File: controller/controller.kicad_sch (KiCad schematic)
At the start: 95 parts, among them J11 Conn_ARM_JTAG_SWD_10, J12 GRPB072VWQS-RC, J13 GRPB072VWQS-RC, J15 Conn_01x03_Pin, J6 USB_C_Receptacle_USB2.0_16P, J7 USB_C_Receptacle_USB2.0_16P, J8 GRPB072VWQS-RC, J9 GRPB072VWQS-RC, Q1 BSS138, Q2 BSS138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

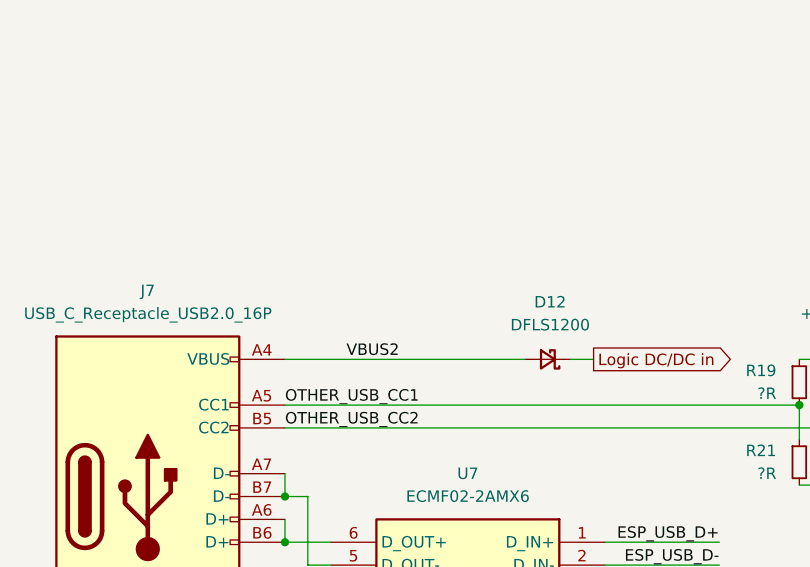
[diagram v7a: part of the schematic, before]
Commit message: Controller - Cleanup and improve silkscreen
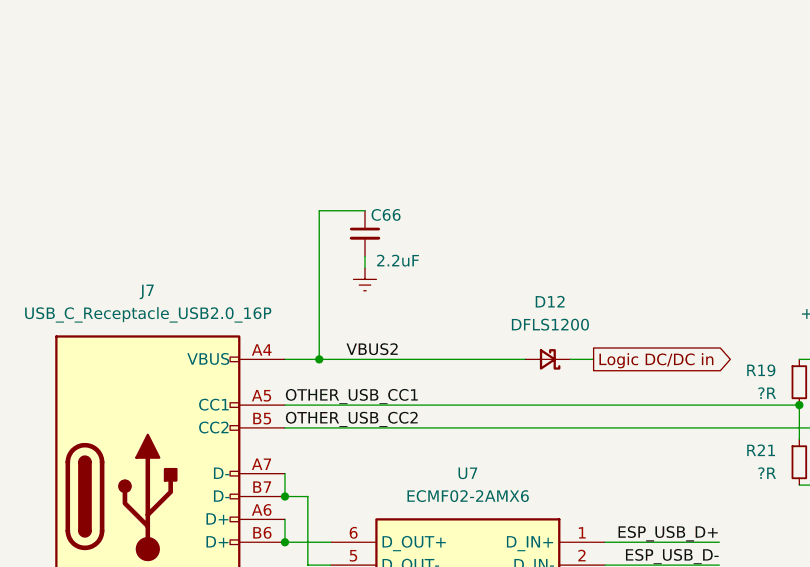
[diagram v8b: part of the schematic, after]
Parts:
- added C66: 2.2uF, Capacitor_SMD:C_0603_1608Metric, symbol Device:C_Small
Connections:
- net Earth: now also C66.2
- net VBUS2: now also C66.1
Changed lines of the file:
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@@
 	)
 	(junction
+		(at 48.26 222.25)
+		(diameter 0)
+		(color 0 0 0 0)
+	)
+	(junction
 		(at 334.01 165.1)
 		(diameter 0)
@@
 	(wire
 		(pts
+			(xy 53.34 210.82) (xy 53.34 212.09)
+		)
+		(stroke
+			(width 0)
+			(type default)
+		)
+	)
+	(wire
+		(pts
 			(xy 147.32 34.29) (xy 163.83 34.29)
 		)
@@
 	(wire
 		(pts
-			(xy 44.45 222.25) (xy 71.12 222.25)
+			(xy 44.45 222.25) (xy 48.26 222.25)
 		)
 		(stroke
@@
 	(wire
 		(pts
+			(xy 53.34 205.74) (xy 48.26 205.74)
+		)
+		(stroke
+			(width 0)
+			(type default)
+		)
+	)
+	(wire
+		(pts
 			(xy 33.02 66.04) (xy 48.26 66.04)
 		)
@@
 	(wire
 		(pts
+			(xy 48.26 205.74) (xy 48.26 222.25)
+		)
+		(stroke
+			(width 0)
+			(type default)
+		)
+	)
+	(wire
+		(pts
 			(xy 45.72 349.25) (xy 45.72 350.52)
 		)
@@
 	(wire
 		(pts
+			(xy 48.26 222.25) (xy 71.12 222.25)
+		)
+		(stroke
+			(width 0)
+			(type default)
+		)
+	)
+	(wire
+		(pts
 			(xy 278.13 275.59) (xy 278.13 278.13)
 		)
@@
 	)
 	(symbol
+		(lib_id "Device:C_Small")
+		(at 53.34 208.28 0)
+		(unit 1)
+		(exclude_from_sim no)
+		(in_bom yes)
+		(on_board yes)
+		(dnp no)
+		(property "Reference" "C66"
+			(at 57.404 206.248 0)
+			(effects
+				(font
+					(size 1.27 1.27)
+				)
+				(justify right)
+			)
+		)
+		(property "Value" "2.2uF"
+			(at 59.436 211.328 0)
+			(effects
+				(font
+					(size 1.27 1.27)
+				)
+				(justify right)
+			)
+		)
+		(property "Footprint" "Capacitor_SMD:C_0603_1608Metric"
+			(at 53.34 208.28 0)
+			(effects
+				(font
+					(size 1.27 1.27)
+				)
+				(hide yes)
+			)
+		)
+		(property "Datasheet" "~"
+			(at 53.34 208.28 0)
+			(effects
+				(font
+					(size 1.27 1.27)
+				)
+				(hide yes)
+			)
+		)
+		(property "Description" "Unpolarized capacitor, small symbol"
+			(at 53.34 208.28 0)
+			(effects
+				(font
+					(size 1.27 1.27)
+				)
+				(hide yes)
+			)
+		)
+		(pin "2"
+		)
+		(pin "1"
+		)
+		(instances
+			(project "controller"
+				(path "/5b092a03-7e3e-4df1-ad91-2ac0e362f857"
+					(reference "C66")
+					(unit 1)
+				)
+			)
+		)
+	)
+	(symbol
 		(lib_id "power:Earth")
 		(at 63.5 57.15 0)
@@
 					(unit 1)
 				)
+			)
+		)
+	)
+	(symbol
+		(lib_id "power:Earth")
+		(at 53.34 212.09 0)
+		(unit 1)
+		(exclude_from_sim no)
+		(in_bom yes)
+		(on_board yes)
+		(dnp no)
+		(fields_autoplaced yes)
+		(property "Reference" "#PWR039"
+			(at 53.34 218.44 0)
+			(effects
+				(font
+					(size 1.27 1.27)
+				)
+				(hide yes)
+			)
+		)
+		(property "Value" "Earth"
+			(at 53.34 215.9 0)
+			(effects
+				(font
+					(size 1.27 1.27)
+				)
+				(hide yes)
+			)
+		)
+		(property "Footprint" ""
+			(at 53.34 212.09 0)
+			(effects
+				(font
+					(size 1.27 1.27)
+				)
+				(hide yes)
+			)
+		)
+		(property "Datasheet" "~"
+			(at 53.34 212.09 0)
+			(effects
+				(font
+					(size 1.27 1.27)
+				)
+				(hide yes)
+			)
+		)
+		(property "Description" ""
+			(at 53.34 212.09 0)
+			(effects
+				(font
+					(size 1.27 1.27)
+				)
+				(hide yes)
+			)
+		)
+		(pin "1"
+		)
+		(instances
+			(project "controller"
+				(path "/5b092a03-7e3e-4df1-ad91-2ac0e362f857"
+					(reference "#PWR039")
+					(unit 1)
+				)
